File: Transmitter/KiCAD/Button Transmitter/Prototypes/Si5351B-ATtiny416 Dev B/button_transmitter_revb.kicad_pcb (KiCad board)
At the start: 2 copper layers, 25 x 25 mm, 40 parts, among them J1 Antenna Screw Pad, J2 1.27mm Pogo Pads For Programm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, Q1 MMUN2238LT1G, U1 TPS22919DCK, U2 Si5351B-B-GM1, U3 ATtiny416-M, U4 Case, U5 TLV61070ADBV, Y1 25MHz

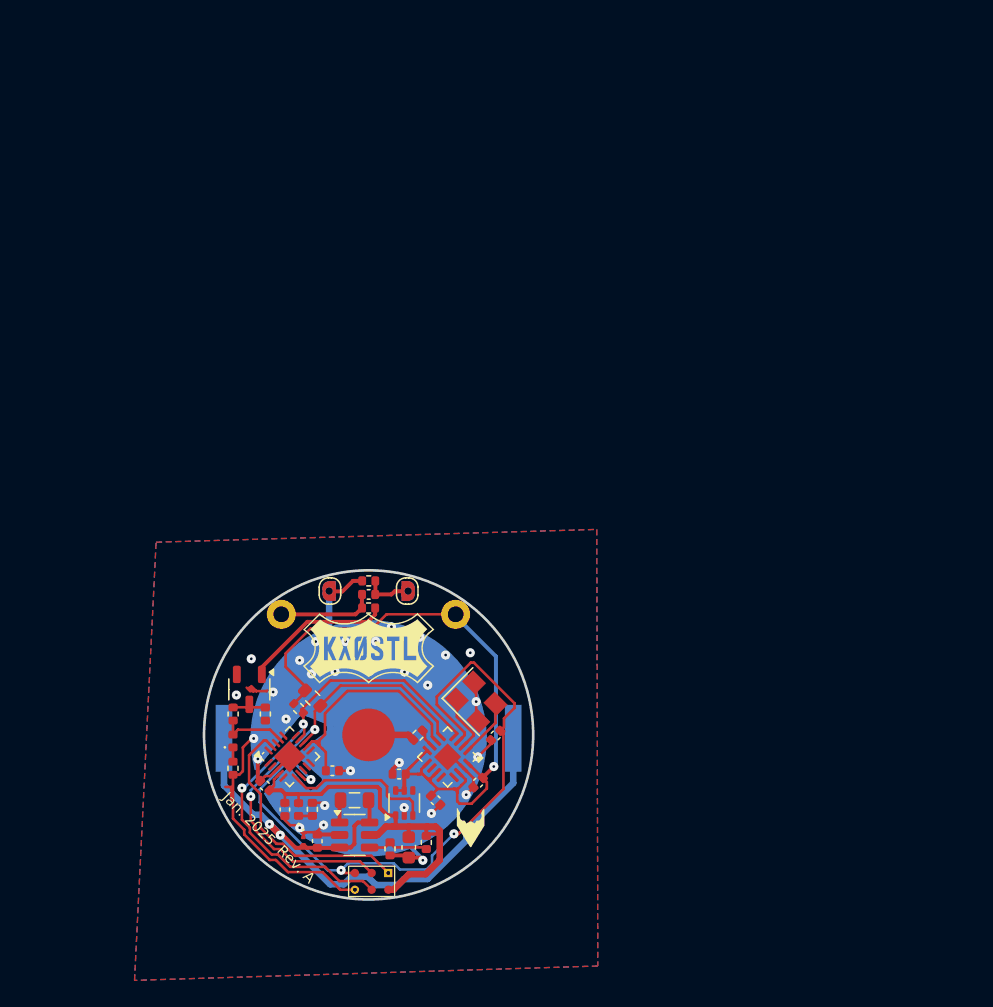
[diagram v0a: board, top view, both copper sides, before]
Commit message: Beginnings of low power boost converter design
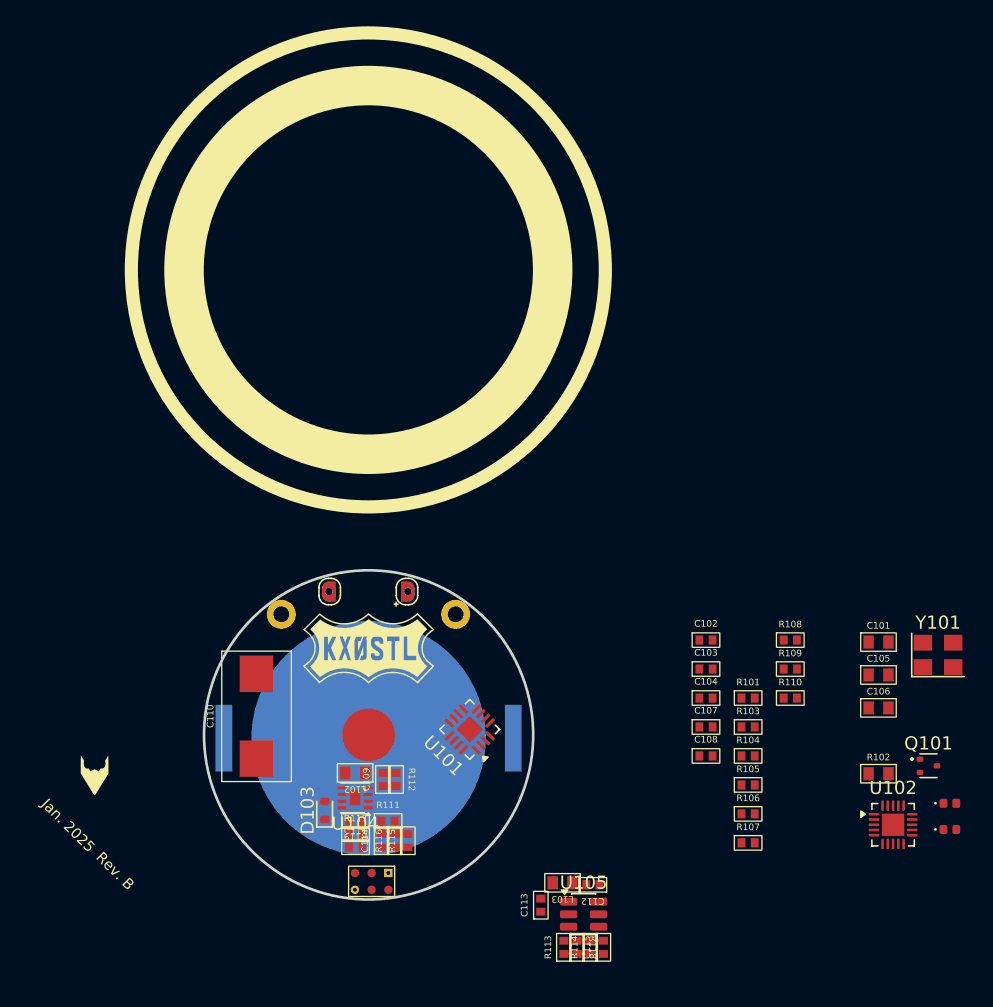
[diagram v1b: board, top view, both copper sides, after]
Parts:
- removed BZ1: 7BB-20-3, Library:Buzzer_Pad_POS
- removed BZ2-1: 7BB-20-3, Library:Buzzer_Pad_NEG
- removed C1, C2, C4, C6, C7, C8: 100nF, Library:Worthington_C_0402_1005Metric
- removed C10: 22uF, Capacitor_SMD:C_0603_1608Metric
- removed C3, C5, C9: 10uF, Library:Worthington_C_0402_1005Metric
- removed D1, D3: RED, Library:Worthington_LED_0402_1005Metric
- removed D2: ESD156B1W, Diode_SMD:D_0201_0603Metric
- removed J1: Antenna Screw Pad, Library:RF_Solder_Pad
- removed L2: 4.7uH, Inductor_SMD:L_0805_2012Metric
- removed Q1: MMUN2238LT1G, Package_TO_SOT_SMD:SOT-23-3
- removed R1: 10k, Library:Worthington_R_0402_1005Metric
- removed R10: 18k, Library:Worthington_R_0402_1005Metric
- removed R11: 100, Library:Worthington_R_0402_1005Metric
- removed R2: 1k8, Resistor_SMD:R_0402_1005Metric
- removed R3: 1k8, Resistor_SMD:R_0603_1608Metric
- removed R4: 0R, Library:Worthington_R_0402_1005Metric
- removed R5, R6: 10, Library:Worthington_R_0402_1005Metric
- removed R7: 1M, Library:Worthington_R_0402_1005Metric
- removed R8: 220, Library:Worthington_R_0402_1005Metric
- removed R9: 100k, Library:Worthington_R_0402_1005Metric
- removed U1: TPS22919DCK, Package_TO_SOT_SMD:SOT-363_SC-70-6
- removed U2: Si5351B-B-GM1, Package_DFN_QFN:QFN-16-1EP_3x3mm_P0.5mm_EP1.45x1.45mm
- removed U3: ATtiny416-M, Package_DFN_QFN:VQFN-20-1EP_3x3mm_P0.4mm_EP1.7x1.7mm
- removed U4: Case, Library:Case_CR2032
- removed U5: TLV61070ADBV, Package_TO_SOT_SMD:SOT-23-6
- removed Y1: 25MHz, Library:Crystal_SMD_Kyocera_CX3225SB-4Pin_3.2x2.5mm
- added BZ101: 7BB-20-3, Library:Buzzer_Pad_POS, F.Cu at (78.6, 93.0)
- added BZ102: 7BB-20-3, Library:Buzzer_Pad_NEG, F.Cu at (72.6, 93.0)
- added C101: 10uF, Library:Worthington_C_0603, F.Cu at (114.3, 96.9)
- added C102: 100nF, Library:Worthington_C_0402, F.Cu at (101.2, 96.7)
- added C103: 100nF, Library:Worthington_C_0402, F.Cu at (101.2, 98.9)
- added C104: 100nF, Library:Worthington_C_0402, F.Cu at (101.2, 101.1)
- added C105: 22uF, Library:Worthington_C_0603, F.Cu at (114.3, 99.4)
- added C106: 22uF, Library:Worthington_C_0603, F.Cu at (114.3, 101.9)
- added C107: 1uF, Library:Worthington_C_0402, F.Cu at (101.2, 103.3)
- added C108: 100nF, Library:Worthington_C_0402, F.Cu at (101.2, 105.5)
- added C109: 1uF, Library:Worthington_C_0402, F.Cu at (76.7, 107.3)
- added C110: 47uF, Library:Worthington_CTant_2917, F.Cu at (67.1, 102.5)
- added C111: 100nF, Library:Worthington_C_0402, F.Cu at (74.6, 112.4)
- added C112: 100nF, Library:Worthington_C_0402, F.Cu at (92.7, 115.3)
- added C113: 100nF, Library:Worthington_C_0402, F.Cu at (88.7, 116.8)
- added C114: 100nF, Library:Worthington_C_0402, F.Cu at (76.6, 112.0)
- added C115: 220pF, Library:Worthington_C_0402, F.Cu at (93.5, 120.0)
- added D101: RED, Library:Worthington_LED_0402_1005Metric, F.Cu at (119.8, 109.1)
- added D102: GREEN, Library:Worthington_LED_0402_1005Metric, F.Cu at (119.8, 111.1)
- added D103: D_Schottky, Diode_SMD:D_SOD-523, F.Cu at (72.3, 109.7)
- added J102: Antenna Spring, Library:RF_Solder_Pad, F.Cu at (75.6, 103.9)
- added L102: 10uH, Library:Worthington_L_0603, F.Cu at (74.6, 106.8)
- added L103: 4u7H, Library:Worthington_L_0603, F.Cu at (90.3, 115.2)
- added Q101: DMN601TK-7, Package_TO_SOT_SMD:SOT-523, F.Cu at (118.1, 106.3)
- added R101: 15k, Library:Worthington_R_0402, F.Cu at (104.4, 101.1)
- added R102: 15k, Library:Worthington_R_0603, F.Cu at (114.3, 106.9)
- added R103: 600, Library:Worthington_R_0402, F.Cu at (104.4, 103.3)
- added R104: 0R, Library:Worthington_R_0402, F.Cu at (104.4, 105.5)
- added R105: 1k, Library:Worthington_R_0402, F.Cu at (104.4, 107.7)
- added R106: 1M, Library:Worthington_R_0402, F.Cu at (104.4, 109.9)
- added R107: 10, Library:Worthington_R_0402, F.Cu at (104.4, 112.1)
- added R108: 10, Library:Worthington_R_0402, F.Cu at (107.6, 96.7)
- added R109: 1M, Library:Worthington_R_0402, F.Cu at (107.6, 98.9)
- added R110: 500, Library:Worthington_R_0402, F.Cu at (107.6, 101.1)
- added R111: 3M, Library:Worthington_R_0402, F.Cu at (77.1, 110.5)
- added R112: 2k2, Library:Worthington_R_0402, F.Cu at (77.7, 107.3)
- added R113: 402k, Library:Worthington_R_0402, F.Cu at (90.5, 120.0)
- added R114: 1k, Library:Worthington_R_0402, F.Cu at (92.5, 120.0)
- added R115: 1k, Library:Worthington_R_0402, F.Cu at (78.6, 112.0)
- added R116: 200k, Library:Worthington_R_0402, F.Cu at (77.6, 112.0)
- added R117: 107k, Library:Worthington_R_0402, F.Cu at (74.6, 111.5)
- added R118: 127k, Library:Worthington_R_0402, F.Cu at (91.5, 120.0)
- added R119: 5k, Library:Worthington_R_0402, F.Cu at (74.6, 110.5)
- added U101: Si5351B-B-GM1, Package_DFN_QFN:QFN-16-1EP_3x3mm_P0.5mm_EP1.45x1.45mm, F.Cu at (83.3, 103.5)
- added U102: ATtiny416-M, Package_DFN_QFN:VQFN-20-1EP_3x3mm_P0.4mm_EP1.7x1.7mm, F.Cu at (115.5, 110.7)
- added U103: Case, Library:Case_CR2032, F.Cu at (75.6, 68.6)
- added U104: MIC2288YML, Package_DFN_QFN:WDFN-8-1EP_2x2mm_P0.5mm_EP0.8x1.2mm, F.Cu at (74.6, 108.7)
- added U105: TPP361081, Package_TO_SOT_SMD:TSOT-23-6, F.Cu at (92.0, 117.5)
- added Y101: 25MHz, Library:Crystal_SMD_Kyocera_CX3225SB-4Pin_3.2x2.5mm, F.Cu at (118.9, 97.8)
- BT101: renamed from BT1; footprint Library:BatteryHolder_Keystone_3034_1x20mm_CUTOUT -> Battery:BatteryHolder_Keystone_3034_1x20mm
- moved G*** 28.8 mm to (54.8, 107.0)
- renumbered J2 to J101, L1 to L101
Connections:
- J101 pad 2: +3V3 -> +2V5
- L101 pad 2: /+3V3_SW -> +2V5
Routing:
- net GND: track 77.7 -> 0.00 mm, vias 30 -> 0
- net /+3V3_SW: track 53.9 -> 0.00 mm, vias 1 -> 0
- net /MCU_DAC0: track 52.9 -> 0.00 mm, vias 3 -> 0
- net Net-(BT101-+): track 48.9 -> 0.00 mm, vias 2 -> 0
- net /MCU_SCL: track 38.9 -> 0.00 mm, vias 2 -> 0
- net /MCU_SDA: track 35.4 -> 0.00 mm, vias 2 -> 0
- net +3V3: track 31.2 -> 0.00 mm
- net /MCU_UPDI: track 19.4 -> 0.00 mm
- net /~{TX_EN}: track 18.0 -> 0.00 mm
- net /OUTPUT_PWR_EN: track 11.6 -> 0.00 mm
- net Net-(Q1-D): track 11.3 -> 0.00 mm
- net Net-(C107-Pad1): track 7.35 -> 0.00 mm
- net /BUZZER_PULSE: track 5.11 -> 0.00 mm
- net Net-(U5-V_{FB}): track 4.68 -> 0.00 mm
- net Net-(U2-XA): track 4.42 -> 0.00 mm
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- removed copper zone on B.Cu, net GND
- removed copper zone on F.Cu, net GND
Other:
- copper layers 2 -> 4
- board text added: "Rev. B"
- board text removed: "Rev. A"
